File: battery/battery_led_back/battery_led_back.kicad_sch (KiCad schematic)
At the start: 14 parts

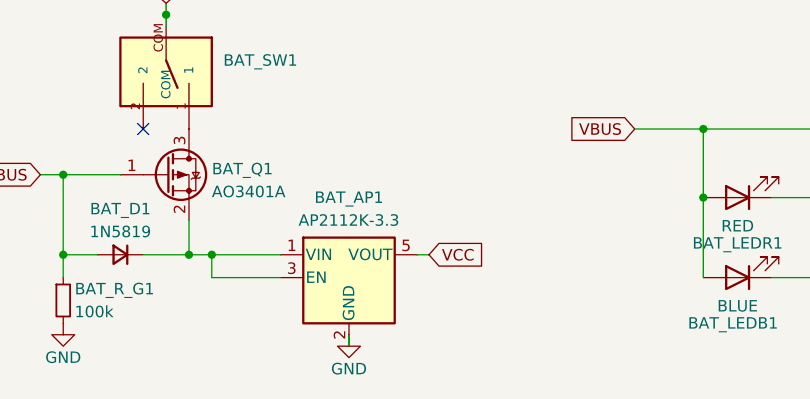
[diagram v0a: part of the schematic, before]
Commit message: add RGB WS2812B modules
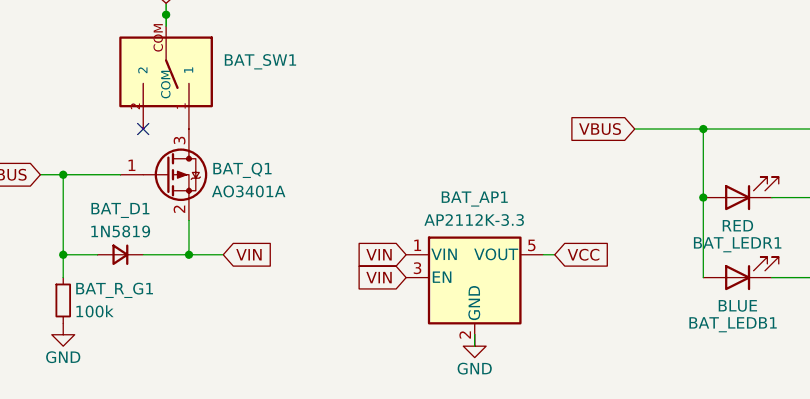
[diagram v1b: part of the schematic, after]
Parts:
- BAT_SW1: value (none) -> ~
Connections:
- net VIN: now reaches BAT_AP1.1 (VIN), BAT_AP1.3 (EN), BAT_D1.1 (K), BAT_Q1.2 (S)
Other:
- moved on the sheet: BAT_AP1

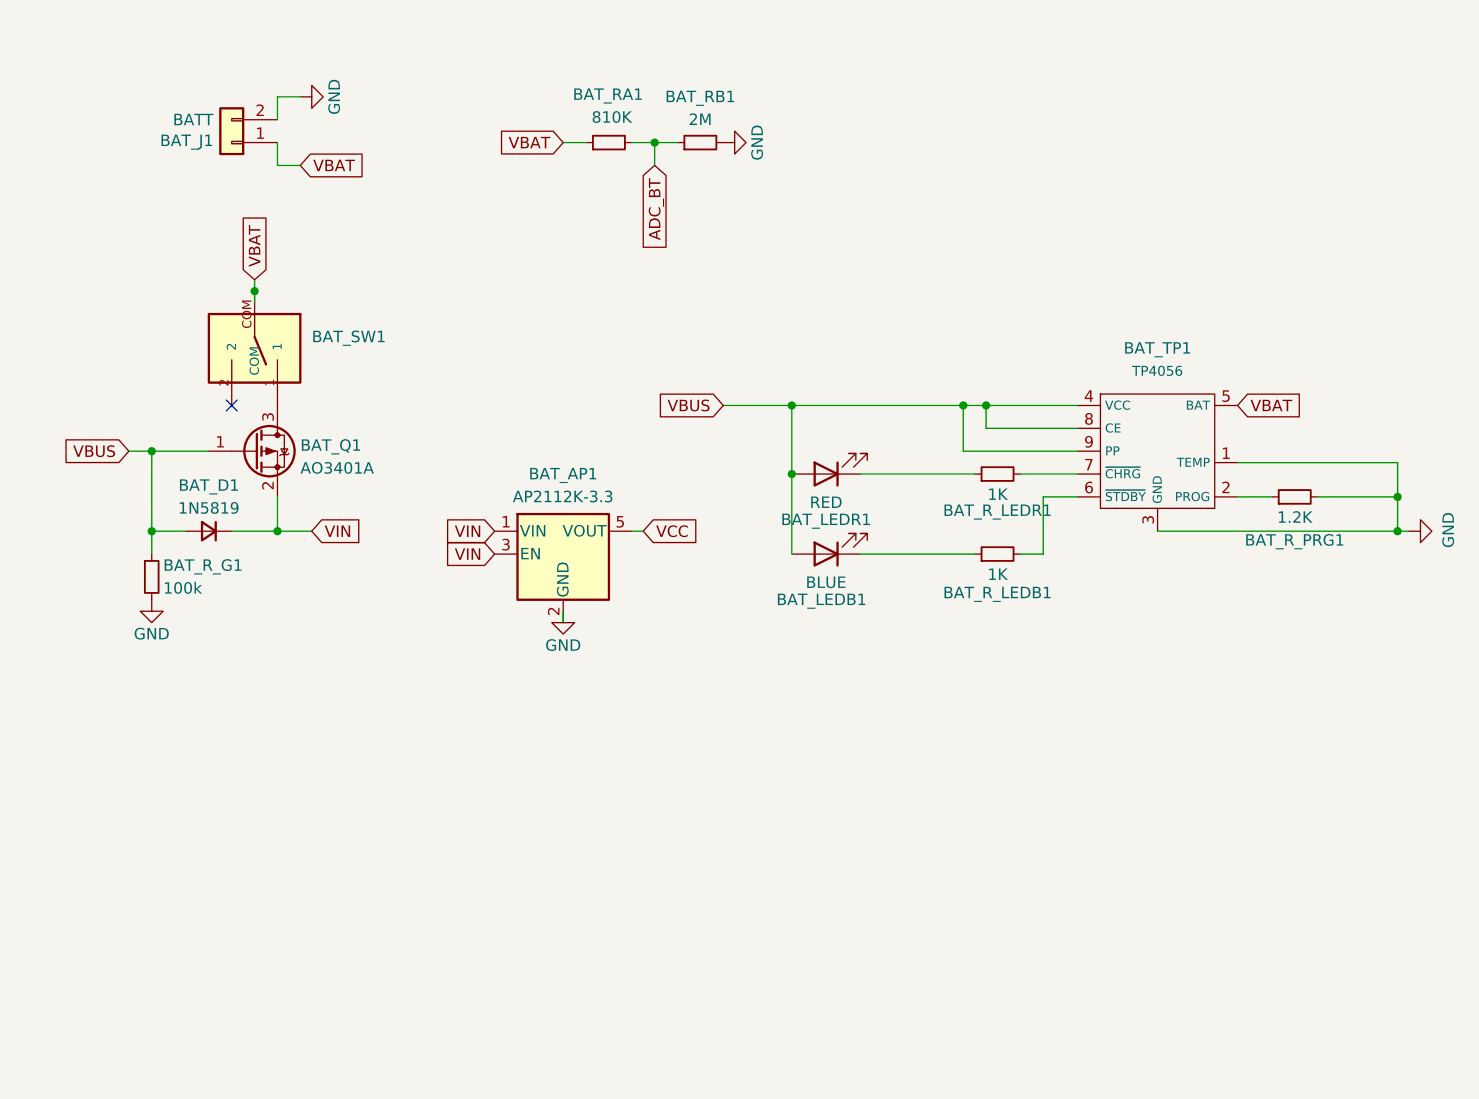
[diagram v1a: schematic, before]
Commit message: use SY8088AAC in battery modules
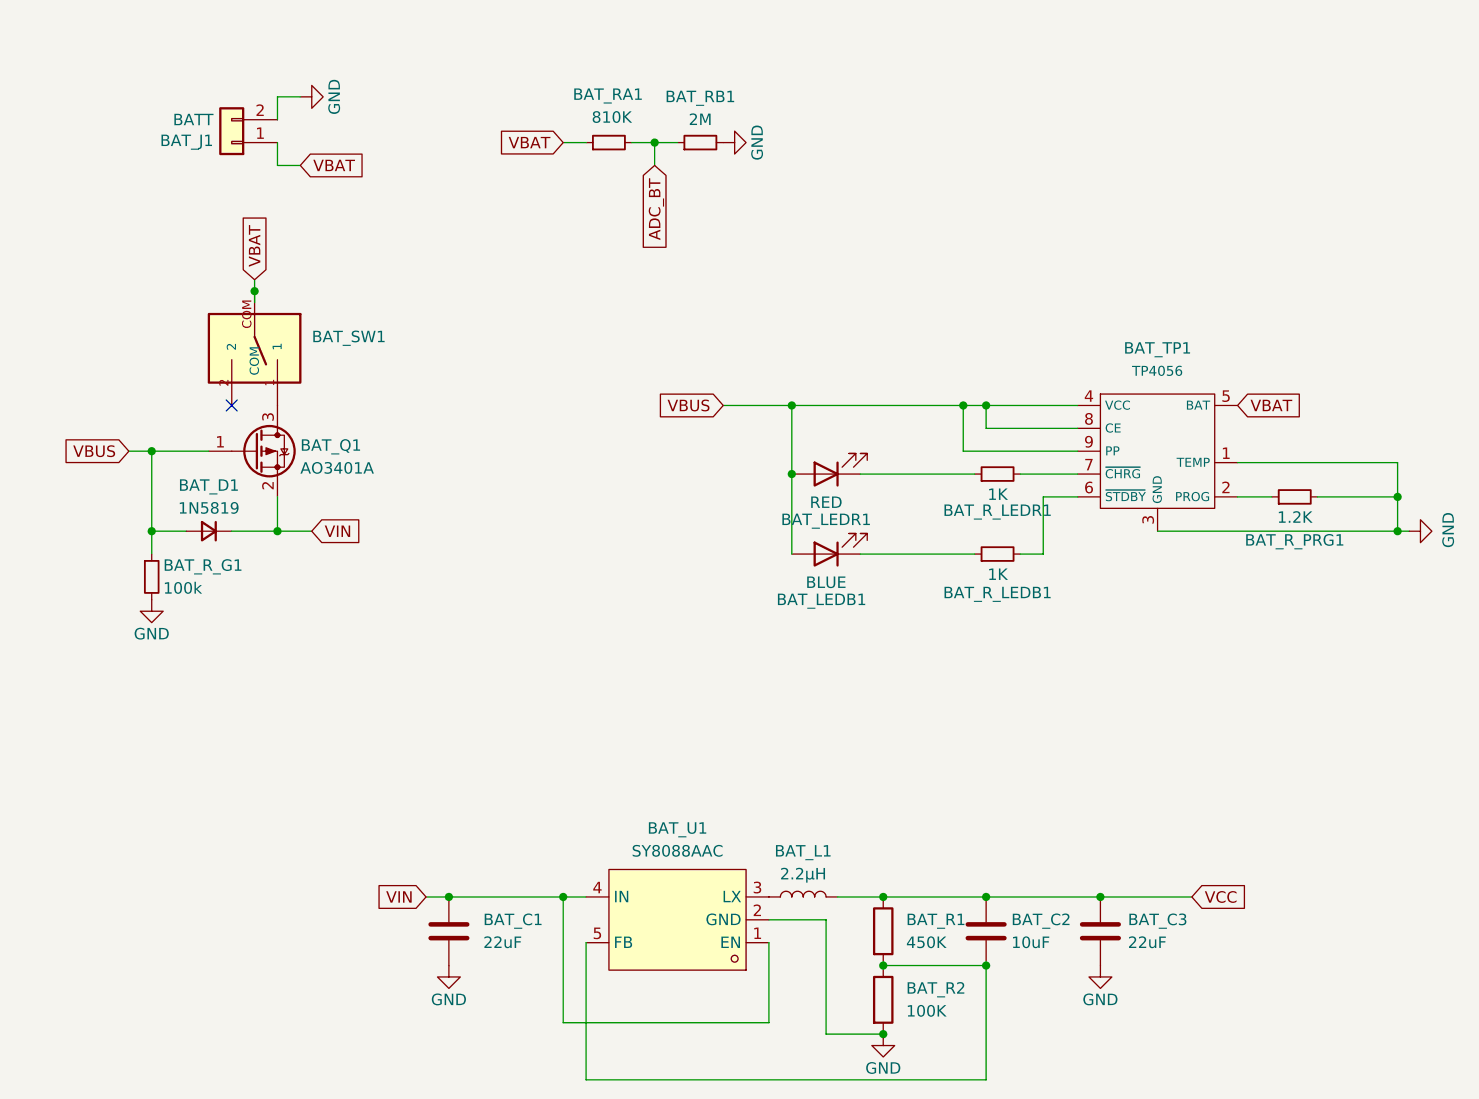
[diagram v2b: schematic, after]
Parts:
- removed BAT_AP1: AP2112K-3.3, ErgoCai.pretty:SOT-23-5, symbol ErgoCai:AP2112K-3.3
- added BAT_C1, BAT_C3: 22uF, Capacitor_SMD:C_0603_1608Metric, symbol Device:C
- added BAT_C2: 10uF, Capacitor_SMD:C_0603_1608Metric, symbol Device:C
- added BAT_L1: 2.2µH, Inductor_SMD:L_0603_1608Metric, symbol Device:L
- added BAT_R1: 450K, ErgoCai.pretty:R_0603_1608Metric, symbol Device:R
- added BAT_R2: 100K, ErgoCai.pretty:R_0603_1608Metric, symbol Device:R
- added BAT_U1: SY8088AAC, ErgoCai.pretty:SOT-23-5_L3.0-W1.7-P0.95-LS2.8-BR, symbol easyeda2kicad:SY8088AAC
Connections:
- net GND: now also BAT_C1.2, BAT_C3.2, BAT_R2.2, BAT_U1.2 (GND)
- net VCC: now also BAT_C2.1, BAT_C3.1, BAT_L1.2, BAT_R1.1
- net VIN: now also BAT_C1.1, BAT_U1.1 (EN), BAT_U1.4 (IN)
- new net: BAT_L1.1, BAT_U1.3 (LX)
- new net: BAT_C2.2, BAT_R1.2, BAT_R2.1, BAT_U1.5 (FB)

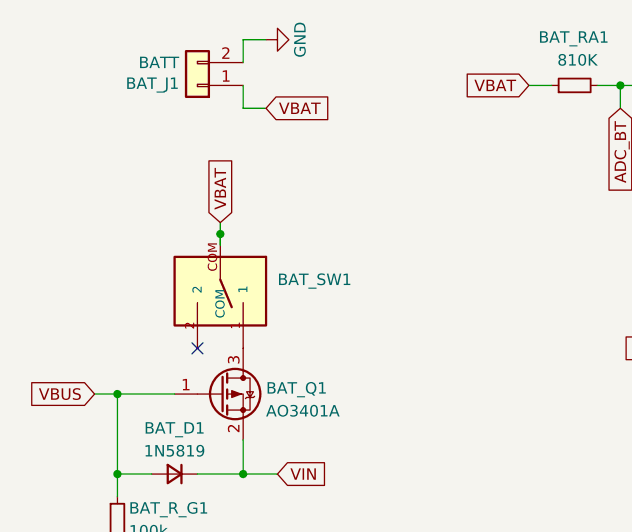
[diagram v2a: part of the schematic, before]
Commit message: update battery switch symbol
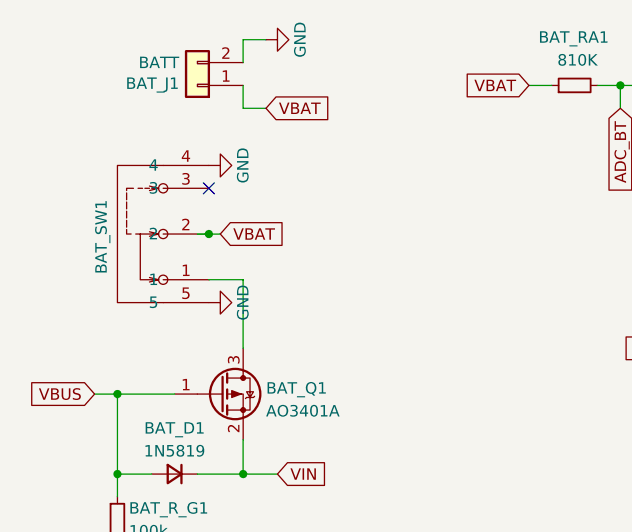
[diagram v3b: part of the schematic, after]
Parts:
- BAT_Q1: footprint ErgoCai.pretty:SOT-23 -> Package_TO_SOT_SMD:SOT-23
- BAT_SW1: footprint ErgoCai.pretty:SK12D07VG4 -> easyeda2kicad:SW-TH_SK12D07VG4; LCSC Part (none) -> C393937
- BAT_TP1: footprint ErgoCai.pretty:SOIC-8-1EP_3.9x4.9mm_P1.27mm_EP2.29x3mm -> Package_SO:SOIC-8-1EP_3.9x4.9mm_P1.27mm_EP2.29x3mm
- BAT_U1: footprint ErgoCai.pretty:SOT-23-5_L3.0-W1.7-P0.95-LS2.8-BR -> easyeda2kicad:SOT-23-5_L3.0-W1.7-P0.95-LS2.8-BR
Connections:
- net GND: now also BAT_SW1.4, BAT_SW1.5
- net VBAT: now also BAT_SW1.2; no longer BAT_SW1.COM
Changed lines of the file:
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@@
 	)
 	(junction
-		(at 85.09 62.23)
+		(at 83.82 62.23)
 		(diameter 0)
 		(color 0 0 0 0)
@@
 	)
 	(no_connect
-		(at 82.55 74.93)
+		(at 83.82 57.15)
 	)
 	(wire
@@
 	(wire
 		(pts
+			(xy 83.82 67.31) (xy 87.63 67.31)
+		)
+		(stroke
+			(width 0)
+			(type default)
+		)
+	)
+	(wire
+		(pts
 			(xy 154.94 137.16) (xy 166.37 137.16)
 		)
@@
 	(wire
 		(pts
+			(xy 87.63 67.31) (xy 87.63 74.93)
+		)
+		(stroke
+			(width 0)
+			(type default)
+		)
+	)
+	(wire
+		(pts
 			(xy 212.09 81.28) (xy 212.09 85.09)
 		)
@@
 	(wire
 		(pts
-			(xy 85.09 62.23) (xy 85.09 60.96)
+			(xy 83.82 62.23) (xy 85.09 62.23)
 		)
 		(stroke
@@
 	(wire
 		(pts
-			(xy 85.09 63.5) (xy 85.09 62.23)
+			(xy 82.55 62.23) (xy 83.82 62.23)
 		)
 		(stroke
@@
 	(global_label "VBAT"
 		(shape input)
-		(at 85.09 60.96 90)
+		(at 85.09 62.23 0)
 		(fields_autoplaced yes)
 		(effects
@@
 		)
 		(property "Intersheetrefs" "${INTERSHEET_REFS}"
-			(at 85.09 53.56 90)
+			(at 92.49 62.23 0)
 			(effects
 				(font
@@
 			)
 		)
-		(property "Footprint" "ErgoCai.pretty:SOT-23-5_L3.0-W1.7-P0.95-LS2.8-BR"
+		(property "Footprint" "easyeda2kicad:SOT-23-5_L3.0-W1.7-P0.95-LS2.8-BR"
 			(at 132.08 121.92 0)
 			(effects
@@
 	(symbol
 		(lib_id "ErgoCai:SK12D07VG4")
-		(at 85.09 67.31 180)
+		(at 78.74 62.23 90)
 		(unit 1)
 		(exclude_from_sim no)
@@
 		(on_board yes)
 		(dnp no)
-		(fields_autoplaced yes)
 		(property "Reference" "BAT_SW1"
-			(at 91.44 67.3099 0)
+			(at 71.882 58.42 0)
 			(effects
 				(font
@@
 		)
 		(property "Value" "~"
-			(at 91.44 69.8499 0)
+			(at 76.2001 68.58 0)
 			(effects
 				(font
@@
 			)
 		)
-		(property "Footprint" "ErgoCai.pretty:SK12D07VG4"
-			(at 85.09 67.31 0)
+		(property "Footprint" "easyeda2kicad:SW-TH_SK12D07VG4"
+			(at 78.74 62.23 0)
 			(effects
 				(font
@@
 			)
 		)
-		(property "Datasheet" "~"
-			(at 85.09 67.31 0)
+		(property "Datasheet" "https://lcsc.com/product-detail/Toggle-Switches_SHOU-HAN-SK12D07VG4_C393937.html"
+			(at 78.74 62.23 0)
 			(effects
 				(font
@@
 		)
 		(property "Description" "Switch, dual pole double throw, separate symbols"
-			(at 85.09 67.31 0)
+			(at 78.74 62.23 0)
 			(effects
 				(font
@@
 		)
 		(property "MF" "C&K"
-			(at 85.09 67.31 0)
+			(at 78.74 62.23 0)
 			(effects
 				(font
@@
 		)
 		(property "Description_1" "Switch Slide ON ON SPDT Side Slide 0.3A 30VDC PC Pins Bracket Mount/Through Hole Bulk"
-			(at 85.09 67.31 0)
+			(at 78.74 62.23 0)
 			(effects
 				(font
@@
 		)
 		(property "Package" "None"
-			(at 85.09 67.31 0)
+			(at 78.74 62.23 0)
 			(effects
 				(font
@@
 		)
 		(property "Price" "None"
-			(at 85.09 67.31 0)
+			(at 78.74 62.23 0)
 			(effects
 				(font
@@
 		)
 		(property "SnapEDA_Link" "https://www.snapeda.com/parts/SK12D07VG4/C%2526K/view-part/?ref=snap"
-			(at 85.09 67.31 0)
+			(at 78.74 62.23 0)
 			(effects
 				(font
@@
 		)
 		(property "MP" "SK12D07VG4"
-			(at 85.09 67.31 0)
+			(at 78.74 62.23 0)
 			(effects
 				(font
@@
 		)
 		(property "Availability" "Not in stock"
-			(at 85.09 67.31 0)
+			(at 78.74 62.23 0)
 			(effects
 				(font
@@
 		)
 		(property "Check_prices" "https://www.snapeda.com/parts/SK12D07VG4/C%2526K/view-part/?ref=eda"
-			(at 85.09 67.31 0)
+			(at 78.74 62.23 0)
 			(effects
 				(font
@@
 			)
 		)
-		(pin "COM"
+		(property "LCSC Part" "C393937"
+			(at 96.52 62.23 0)
+			(effects
+				(font
+					(size 1.27 1.27)
+				)
+				(hide yes)
+			)
+		)
+		(pin "5"
 		)
 		(pin "2"
 		)
 		(pin "1"
+		)
+		(pin "3"
+		)
+		(pin "4"
 		)
 		(instances
@@
 			)
 		)
-		(property "Datasheet" ""
+		(property "Datasheet" "~"
 			(at 106.68 133.35 0)
 			(effects
@@
 			)
 		)
-		(property "Description" ""
+		(property "Description" "Unpolarized capacitor"
 			(at 106.68 133.35 0)
 			(effects
@@
 			)
 		)
+		(property "Sim.Pins" "1=K 2=A"
+			(at 148.59 91.44 0)
+			(effects
+				(font
+					(size 1.27 1.27)
+				)
+				(hide yes)
+			)
+		)
 		(pin "1"
 		)
@@
 			)
 		)
-		(property "Datasheet" ""
+		(property "Datasheet" "~"
 			(at 146.05 129.54 0)
 			(effects
@@
 			)
 		)
-		(property "Description" ""
+		(property "Description" "Inductor"
 			(at 146.05 129.54 0)
 			(effects
@@
 		)
 		(property "Description" "Light emitting diode"
+			(at 148.59 82.55 0)
+			(effects
+				(font
+					(size 1.27 1.27)
+				)
+				(hide yes)
+			)
+		)
+		(property "Sim.Pins" "1=K 2=A"
 			(at 148.59 82.55 0)
 			(effects
@@
 	)
 	(symbol
+		(lib_id "power:GND")
+		(at 83.82 54.61 90)
+		(unit 1)
+		(exclude_from_sim no)
+		(in_bom yes)
+		(on_board yes)
+		(dnp no)
+		(property "Reference" "#PWR05"
+			(at 90.17 54.61 0)
+			(effects
+				(font
+					(size 1.27 1.27)
+				)
+				(hide yes)
+			)
+		)
+		(property "Value" "GND"
+			(at 87.63 54.61 0)
+			(effects
+				(font
+					(size 1.27 1.27)
+				)
+			)
+		)
+		(property "Footprint" ""
+			(at 83.82 54.61 0)
+			(effects
+				(font
+					(size 1.27 1.27)
+				)
+				(hide yes)
+			)
+		)
+		(property "Datasheet" ""
+			(at 83.82 54.61 0)
+			(effects
+				(font
+					(size 1.27 1.27)
+				)
+				(hide yes)
+			)
+		)
+		(property "Description" "Power symbol creates a global label with name \"GND\" , ground"
+			(at 83.82 54.61 0)
+			(effects
+				(font
+					(size 1.27 1.27)
+				)
+				(hide yes)
+			)
+		)
+		(pin "1"
+		)
+		(instances
+			(project "battery_led_back"
+				(path "/5ac02cf2-291a-487e-b868-5e66ea14e5ba"
+					(reference "#PWR05")
+					(unit 1)
+				)
+			)
+		)
+	)
+	(symbol
+		(lib_id "power:GND")
+		(at 83.82 69.85 90)
+		(unit 1)
+		(exclude_from_sim no)
+		(in_bom yes)
+		(on_board yes)
+		(dnp no)
+		(property "Reference" "#PWR04"
+			(at 90.17 69.85 0)
+			(effects
+				(font
+					(size 1.27 1.27)
+				)
+				(hide yes)
+			)
+		)
+		(property "Value" "GND"
+			(at 87.63 69.85 0)
+			(effects
+				(font
+					(size 1.27 1.27)
+				)
+			)
+		)
+		(property "Footprint" ""
+			(at 83.82 69.85 0)
+			(effects
+				(font
+					(size 1.27 1.27)
+				)
+				(hide yes)
+			)
+		)
+		(property "Datasheet" ""
+			(at 83.82 69.85 0)
+			(effects
+				(font
+					(size 1.27 1.27)
+				)
+				(hide yes)
+			)
+		)
+		(property "Description" "Power symbol creates a global label with name \"GND\" , ground"
+			(at 83.82 69.85 0)
+			(effects
+				(font
+					(size 1.27 1.27)
+				)
+				(hide yes)
+			)
+		)
+		(pin "1"
+		)
+		(instances
+			(project "battery_led_back"
+				(path "/5ac02cf2-291a-487e-b868-5e66ea14e5ba"
+					(reference "#PWR04")
+					(unit 1)
+				)
+			)
+		)
+	)
+	(symbol
 		(lib_id "Device:R_Small")
 		(at 73.66 93.98 0)
@@
 			)
 		)
-		(property "Footprint" "ErgoCai.pretty:SOT-23"
+		(property "Footprint" "Package_TO_SOT_SMD:SOT-23"
 			(at 90.17 81.915 0)
 			(effects
@@
 			)
 		)
-		(property "Datasheet" ""
+		(property "Datasheet" "~"
 			(at 166.37 133.35 0)
 			(effects
@@
 			)
 		)
-		(property "Description" ""
+		(property "Description" "Unpolarized capacitor"
 			(at 166.37 133.35 0)
 			(effects
@@
 			)
 		)
-		(property "Datasheet" ""
+		(property "Datasheet" "~"
 			(at 179.07 133.35 0)
 			(effects
@@
 			)
 		)
-		(property "Description" ""
+		(property "Description" "Unpolarized capacitor"
 			(at 179.07 133.35 0)
 			(effects
@@
 			)
 		)
-		(property "Footprint" "ErgoCai.pretty:SOIC-8-1EP_3.9x4.9mm_P1.27mm_EP2.29x3mm"
+		(property "Footprint" "Package_SO:SOIC-8-1EP_3.9x4.9mm_P1.27mm_EP2.29x3mm"
 			(at 179.07 86.36 0)
 			(effects

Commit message: remove default battery
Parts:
- BAT_C1, BAT_C2, BAT_C3: footprint Capacitor_SMD:C_0603_1608Metric -> ErgoCai.pretty:C_0603_1608Metric
- BAT_L1: footprint Inductor_SMD:L_0603_1608Metric -> ErgoCai.pretty:L_0603_1608Metric
- BAT_Q1: footprint Package_TO_SOT_SMD:SOT-23 -> ErgoCai.pretty:SOT-23
- BAT_SW1: footprint easyeda2kicad:SW-TH_SK12D07VG4 -> ErgoCai.pretty:SW-TH_SK12D07VG4
- BAT_TP1: footprint Package_SO:SOIC-8-1EP_3.9x4.9mm_P1.27mm_EP2.29x3mm -> ErgoCai.pretty:SOIC-8-1EP_3.9x4.9mm_P1.27mm_EP2.29x3mm
- BAT_U1: footprint easyeda2kicad:SOT-23-5_L3.0-W1.7-P0.95-LS2.8-BR -> ErgoCai.pretty:SOT-23-5_L3.0-W1.7-P0.95-LS2.8-BR
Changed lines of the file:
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@@
 			)
 		)
-		(property "Footprint" "easyeda2kicad:SOT-23-5_L3.0-W1.7-P0.95-LS2.8-BR"
+		(property "Footprint" "ErgoCai.pretty:SOT-23-5_L3.0-W1.7-P0.95-LS2.8-BR"
 			(at 132.08 121.92 0)
 			(effects
@@
 			)
 		)
-		(property "Footprint" "easyeda2kicad:SW-TH_SK12D07VG4"
+		(property "Footprint" "ErgoCai.pretty:SW-TH_SK12D07VG4"
 			(at 78.74 62.23 0)
 			(effects
@@
 			)
 		)
-		(property "Footprint" "Capacitor_SMD:C_0603_1608Metric"
+		(property "Footprint" "ErgoCai.pretty:C_0603_1608Metric"
 			(at 107.6452 137.16 0)
 			(effects
@@
 			)
 		)
-		(property "Footprint" "Inductor_SMD:L_0603_1608Metric"
+		(property "Footprint" "ErgoCai.pretty:L_0603_1608Metric"
 			(at 146.05 129.54 0)
 			(effects
@@
 			)
 		)
-		(property "Footprint" "Package_TO_SOT_SMD:SOT-23"
+		(property "Footprint" "ErgoCai.pretty:SOT-23"
 			(at 90.17 81.915 0)
 			(effects
@@
 			)
 		)
-		(property "Footprint" "Capacitor_SMD:C_0603_1608Metric"
+		(property "Footprint" "ErgoCai.pretty:C_0603_1608Metric"
 			(at 167.3352 137.16 0)
 			(effects
@@
 			)
 		)
-		(property "Footprint" "Capacitor_SMD:C_0603_1608Metric"
+		(property "Footprint" "ErgoCai.pretty:C_0603_1608Metric"
 			(at 180.0352 137.16 0)
 			(effects
@@
 			)
 		)
-		(property "Footprint" "Package_SO:SOIC-8-1EP_3.9x4.9mm_P1.27mm_EP2.29x3mm"
+		(property "Footprint" "ErgoCai.pretty:SOIC-8-1EP_3.9x4.9mm_P1.27mm_EP2.29x3mm"
 			(at 179.07 86.36 0)
 			(effects

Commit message: add power switch
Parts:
- removed BAT_SW1: ~, ErgoCai.pretty:SW-TH_SK12D07VG4, symbol ErgoCai:SK12D07VG4
- renumbered BAT_R_PRG1 to BAT_R_P1
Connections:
- net VSYS: now reaches BAT_Q1.3 (D)
- no-connect marks 1 -> 0
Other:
- moved on the sheet: BAT_C1, BAT_C2, BAT_C3, BAT_D1, BAT_J1, BAT_L1, BAT_LEDB1, BAT_LEDR1, BAT_Q1, BAT_R1, BAT_R2, BAT_RA1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

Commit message: update to 3.3V tag
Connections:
- net VCC renamed 3.3V
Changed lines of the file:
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@@
 		)
 	)
-	(global_label "VCC"
+	(global_label "3.3V"
 		(shape input)
 		(at 187.96 123.19 0)
@@
 		)
 		(property "Intersheetrefs" "${INTERSHEET_REFS}"
-			(at 194.5738 123.19 0)
+			(at 195.0576 123.19 0)
 			(effects
 				(font
